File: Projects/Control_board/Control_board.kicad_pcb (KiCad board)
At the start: 2 copper layers, 99.5 x 100.4 mm, 68 parts, among them IC1 VN7050ASTR, IC2 PCA9615DPJ, IC3 PSSI2021SAY,115, J1 66200621022, J10 43045-0401, J11 Conn_01x04, J12 Conn_01x04, J13 Conn_01x01_Female, J2 66200621022, J3 43045-0200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

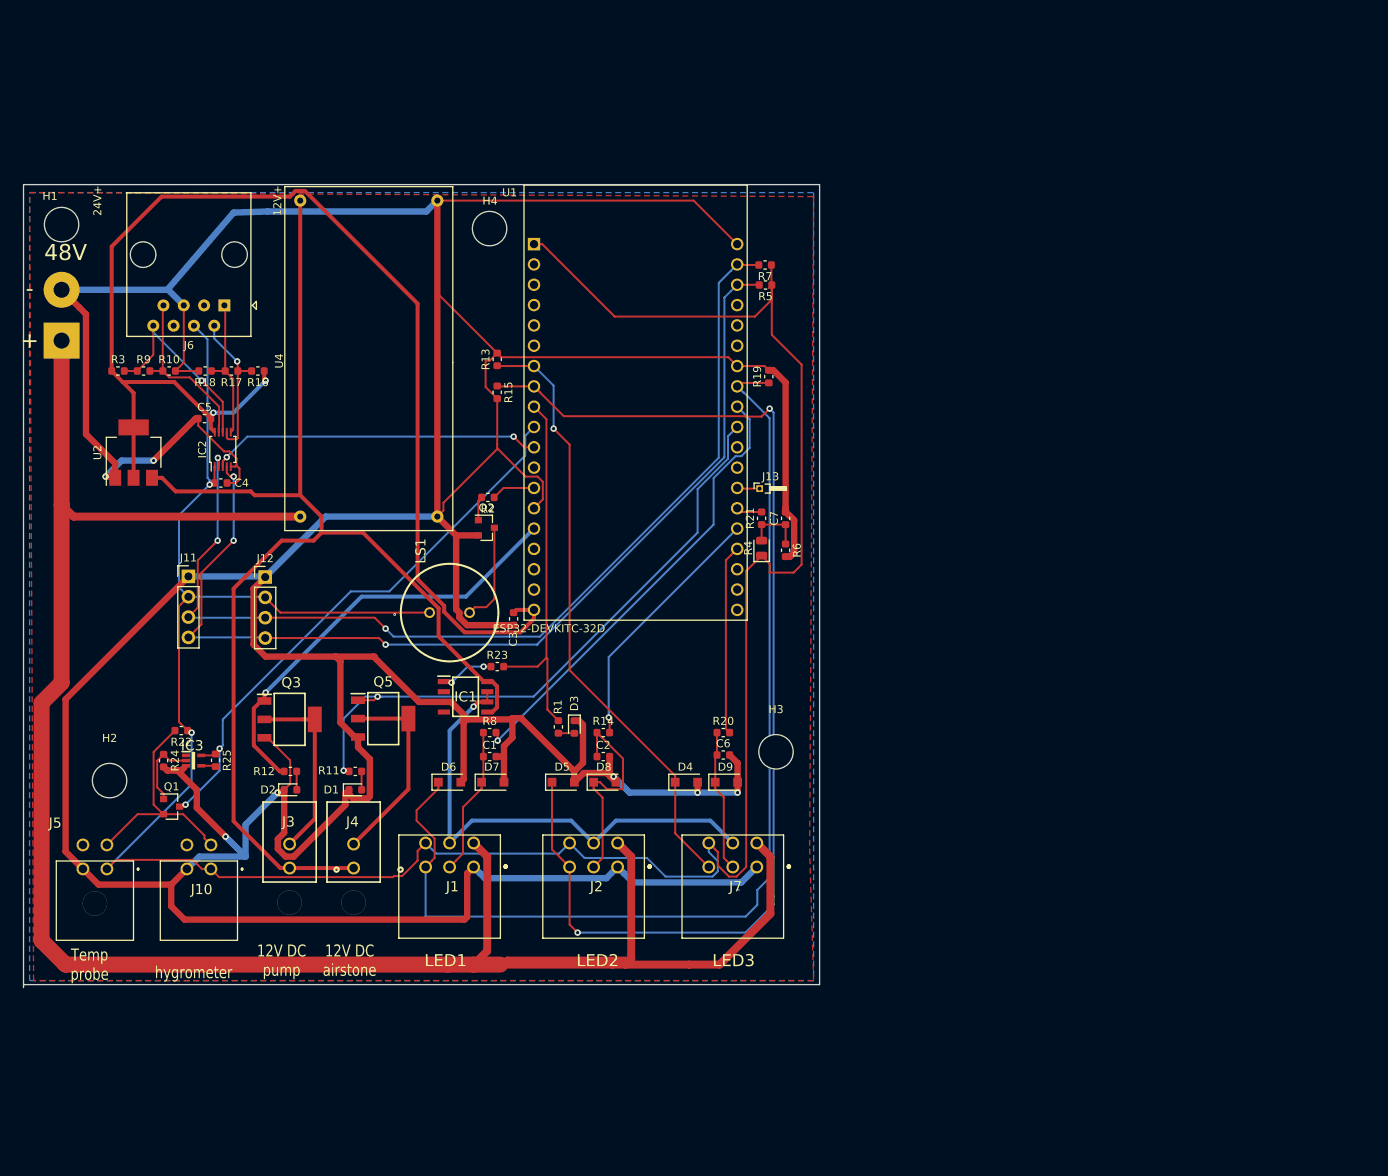
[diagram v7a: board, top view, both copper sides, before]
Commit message: updated with reverse polarity protection
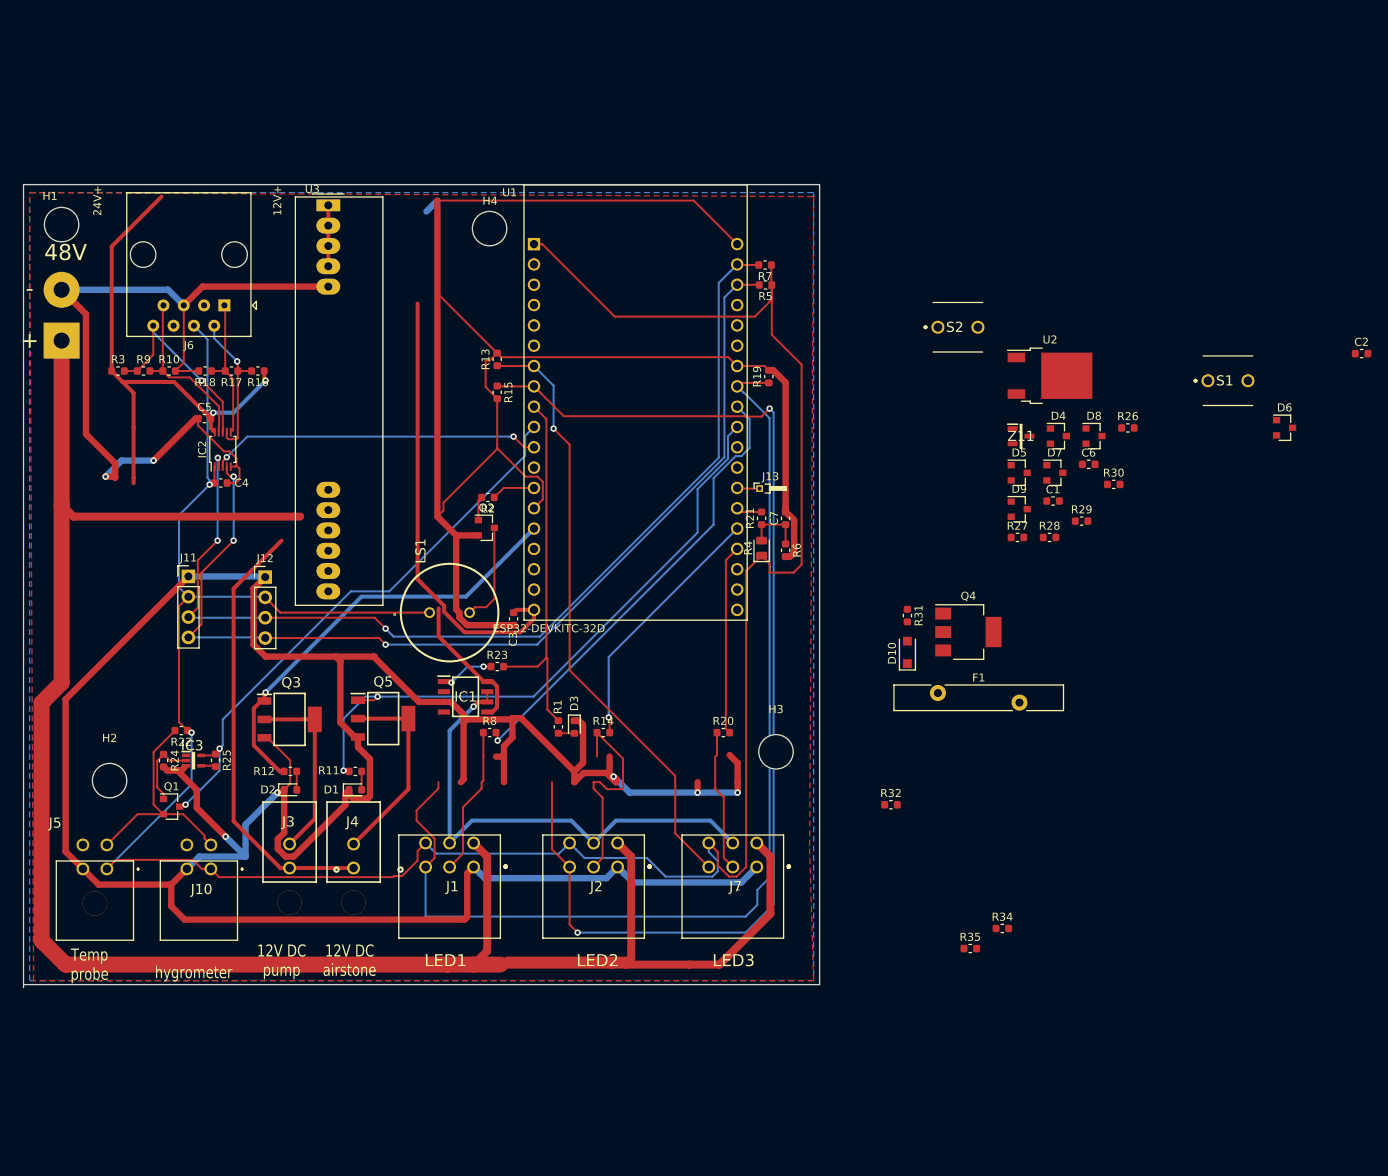
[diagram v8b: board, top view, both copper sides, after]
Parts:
- removed U4: DCDC_lm2596, Kicad_mylib:LM2596_module
- added D10: SMF60A, Diode_SMD:D_SOD-123F, F.Cu at (189.2, 141.0)
- added F1: Polyfuse, Fuse:Fuse_Bourns_MF-RHT1100, F.Cu at (193.0, 146.1)
- added Q4: Q_PMOS_GDS, Package_TO_SOT_SMD:SOT-223-3_TabPin2, F.Cu at (196.8, 138.4)
- added R26: 1k, Resistor_SMD:R_0603_1608Metric, F.Cu at (216.8, 112.9)
- added R27: 1k, Resistor_SMD:R_0603_1608Metric, F.Cu at (203.0, 126.6)
- added R28: 10K, Resistor_SMD:R_0603_1608Metric, F.Cu at (207.0, 126.6)
- added R29: 10K, Resistor_SMD:R_0603_1608Metric, F.Cu at (211.0, 124.6)
- added R30: 1k, Resistor_SMD:R_0603_1608Metric, F.Cu at (215.0, 120.0)
- added R31: 100k, Resistor_SMD:R_0603_1608Metric, F.Cu at (189.2, 136.4)
- added R32: DNP, Resistor_SMD:R_0603_1608Metric, F.Cu at (187.2, 160.0)
- added R34: DNP, Resistor_SMD:R_0603_1608Metric, F.Cu at (201.1, 175.5)
- added R35: DNP, Resistor_SMD:R_0603_1608Metric, F.Cu at (197.1, 178.0)
- added S1: FSM8JRT, SamacSys_Parts:FSM8JRT, F.Cu at (226.8, 107.0)
- added S2: FSM8JRT, SamacSys_Parts:FSM8JRT, F.Cu at (193.0, 100.3)
- added U3: NID35-12_meanwell, Converter_DCDC:Converter_DCDC_MeanWell_NID30_THT, F.Cu at (116.8, 85.1)
- added Z11: BZX84C8V2LT1G, SamacSys_Parts:SOT95P237X111-3N, F.Cu at (203.4, 114.0)
- C1, C2, C6: value 100nF -> 0.1uF
- D4, D5, D6, D7, D8, D9: value SMF5.0A -> BAT54S; footprint Diode_SMD:D_SOD-123F -> Package_TO_SOT_SMD:SOT-23
- R14, R20, R8: value 100 -> 1k
- U2: value NCP1117-5.0_SOT223 -> NCP1117-5.0_TO252; footprint Package_TO_SOT_SMD:SOT-223-3_TabPin2 -> Package_TO_SOT_SMD:TO-252-2
- moved U2 115.0 mm to (207.1, 106.4), turned to 0 degrees
- moved D6 113.4 mm to (236.4, 112.9)
- moved C2 107.3 mm to (246.0, 103.6)
- moved D7 80.2 mm to (207.7, 118.5)
- moved C1 77.3 mm to (207.4, 122.1)
- moved D8 74.9 mm to (212.6, 113.9)
- moved D5 68.9 mm to (203.2, 118.5)
- moved D4 63.5 mm to (208.1, 113.9)
- moved C6 58.4 mm to (211.9, 117.5)
- moved D9 50.0 mm to (203.2, 123.1)
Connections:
- C1 pad 1: /ADJ_LED1 -> Net-(C1-Pad1)
- C2 pad 1: /ADJ_LED2 -> Net-(C2-Pad1)
- C6 pad 1: /ADJ_LED3 -> Net-(C6-Pad1)
- D4 pad 1: /NTC_3 -> GND
- D4 pad 2: GND -> +3V3
- D5 pad 1: /NTC_2 -> GND
- D5 pad 2: GND -> +3V3
- D6 pad 1: /NTC_1 -> GND
- D6 pad 2: GND -> +3V3
- D7 pad 1: /ADJ_LED1 -> GND
- D7 pad 2: GND -> +3V3
- D8 pad 1: /ADJ_LED2 -> GND
- D8 pad 2: GND -> +3V3
- D9 pad 1: /ADJ_LED3 -> GND
- D9 pad 2: GND -> +3V3
- IC1 pad 2: (no net) -> Net-(IC1-Pad2)
- IC1 pad 4: (no net) -> Net-(IC1-Pad4)
- IC3 pad 1: (no net) -> Net-(IC3-Pad1)
- J10 pad 4: (no net) -> Net-(J10-Pad4)
- J5 pad 3: Net-(J10-Pad3) -> Net-(J5-Pad3)
- J5 pad 4: (no net) -> Net-(J5-Pad4)
- J6 pad 3: (no net) -> Net-(J6-Pad3)
- J6 pad 6: (no net) -> Net-(J6-Pad6)
- J8 pad 1: +48V -> VCC
- Q1 pad 2: Net-(J10-Pad3) -> Net-(J5-Pad3)
- R13 pad 1: /NTC_3 -> Net-(D4-Pad3)
- R14 pad 2: Net-(R14-Pad2) -> Net-(C2-Pad1)
- R15 pad 1: /NTC_2 -> Net-(D5-Pad3)
- R19 pad 1: /NTC_1 -> Net-(D9-Pad3)
- R20 pad 2: Net-(R20-Pad2) -> Net-(C6-Pad1)
- R22 pad 2: Net-(J10-Pad3) -> Net-(J5-Pad3)
- R8 pad 2: Net-(R8-Pad2) -> Net-(C1-Pad1)
- U1 pad 12: (no net) -> /Spare
- U1 pad 16: (no net) -> Net-(U1-Pad16)
- U1 pad 17: (no net) -> Net-(U1-Pad17)
- U1 pad 18: (no net) -> Net-(U1-Pad18)
- U1 pad 2: (no net) -> Net-(U1-Pad2)
- U1 pad 23: (no net) -> Net-(U1-Pad23)
- U1 pad 24: (no net) -> Net-(U1-Pad24)
- U1 pad 25: (no net) -> Net-(R29-Pad2)
- U1 pad 27: /NTC_1 -> Net-(D9-Pad3)
- U1 pad 28: Net-(R8-Pad2) -> Net-(C1-Pad1)
- U1 pad 3: (no net) -> Net-(U1-Pad3)
- U1 pad 30: (no net) -> Net-(U1-Pad30)
- U1 pad 31: (no net) -> Net-(U1-Pad31)
- U1 pad 34: Net-(R14-Pad2) -> Net-(C2-Pad1)
- U1 pad 35: Net-(R20-Pad2) -> Net-(C6-Pad1)
- U1 pad 36: (no net) -> Net-(U1-Pad36)
- U1 pad 37: (no net) -> Net-(U1-Pad37)
- U1 pad 38: (no net) -> Net-(U1-Pad38)
- U1 pad 4: (no net) -> Net-(U1-Pad4)
- U1 pad 5: (no net) -> Net-(U1-Pad5)
- U1 pad 6: (no net) -> Net-(R28-Pad2)
- U1 pad 7: /NTC_3 -> Net-(D4-Pad3)
- U1 pad 8: /NTC_2 -> Net-(D5-Pad3)
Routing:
- net +12V: track 158.5 -> 80.1 mm
- net Net-(R8-Pad2): track 56.9 -> 0.00 mm, vias 1 -> 0
- net Net-(C1-Pad1): track 0.00 -> 56.9 mm, vias 0 -> 1
- net GND: track 725.5 -> 683.1 mm
- net +5V: track 159.5 -> 121.4 mm
- net Net-(R14-Pad2): track 32.2 -> 0.00 mm, vias 1 -> 0
- net Net-(C2-Pad1): track 0.00 -> 32.2 mm, vias 0 -> 1
- net Net-(R20-Pad2): track 23.7 -> 0.00 mm
- net Net-(C6-Pad1): track 0.00 -> 23.7 mm
